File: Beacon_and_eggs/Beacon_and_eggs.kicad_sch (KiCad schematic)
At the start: 41 parts, among them J1 USB_C_Receptacle_USB2.0_16P, Q1 IRLML0030, SW1 Boot, SW2 Reset, U1 SA818V, U2 STM32F411CEUx, U3 ADXL343, U6 MCP1253-33X50I/MS, U7 MCP1253-33X50I/MS, Y1 25MHz 18pF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

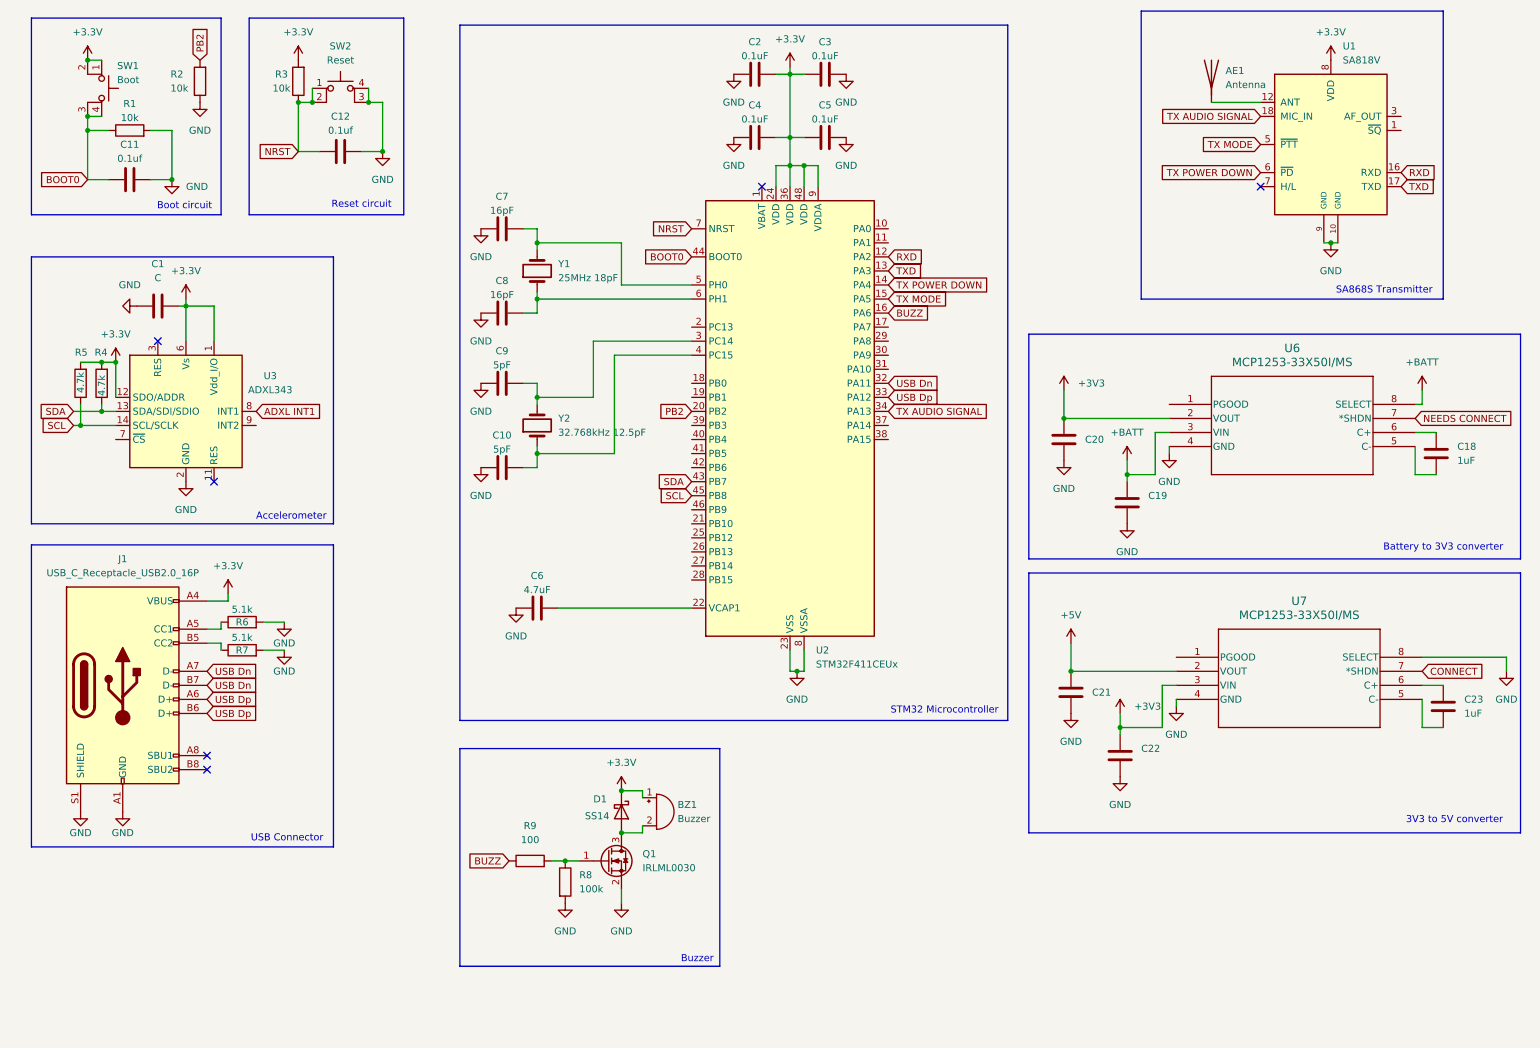
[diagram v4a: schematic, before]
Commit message: relabeled some global tags
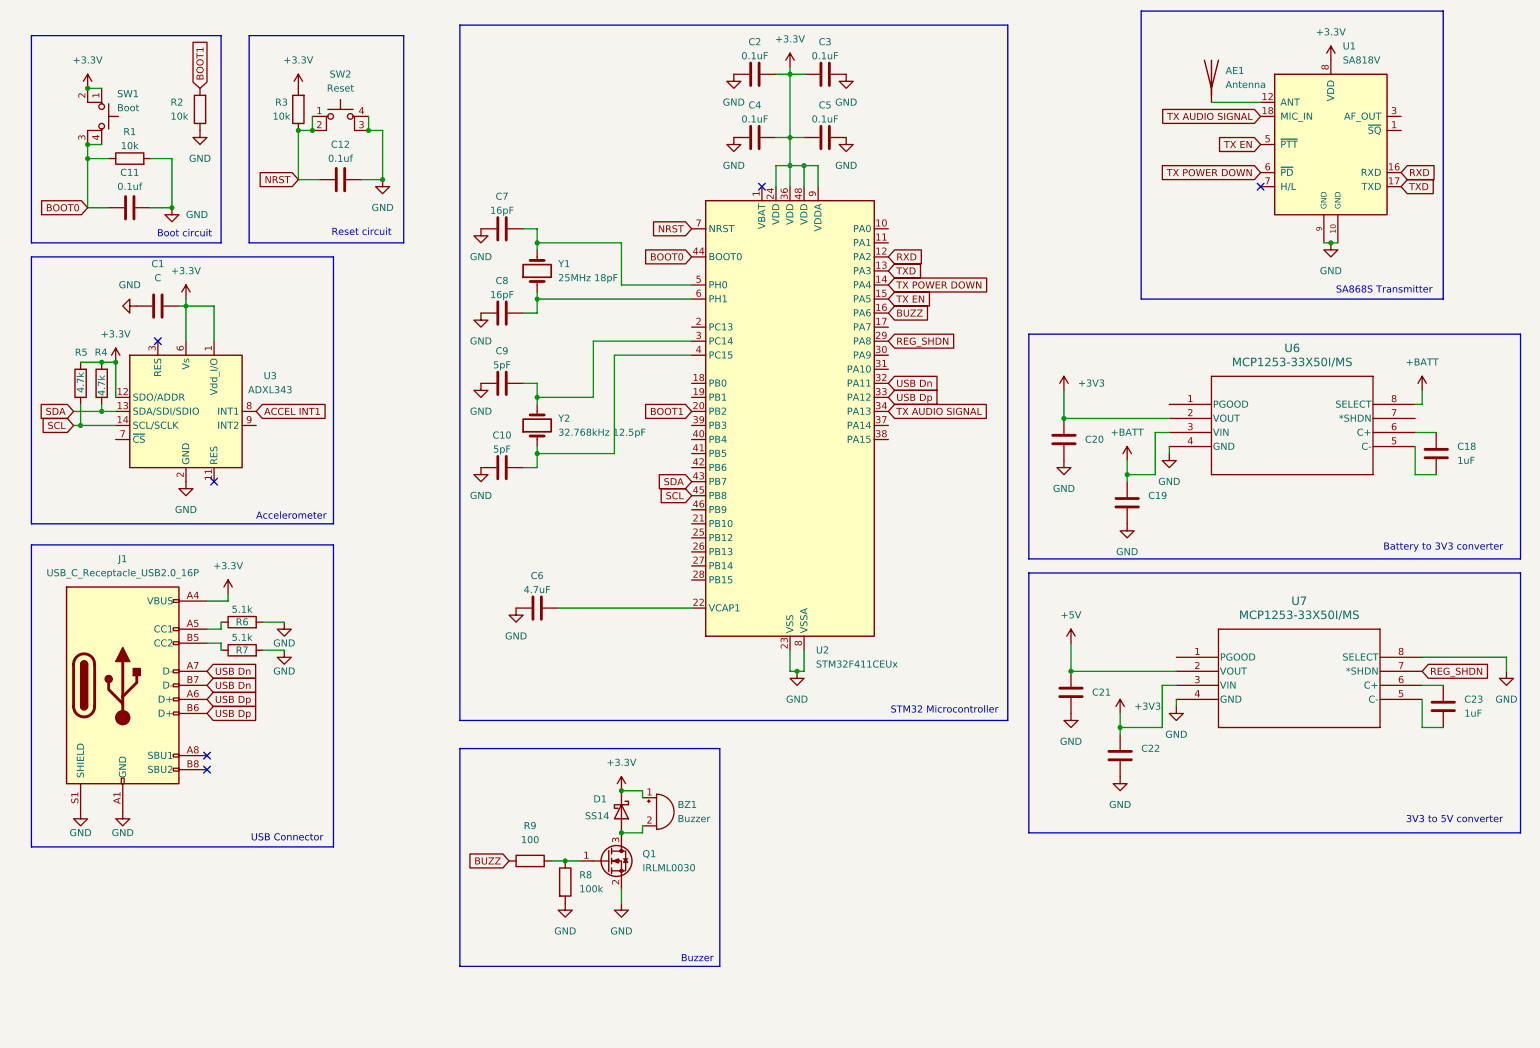
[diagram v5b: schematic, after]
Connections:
- net CONNECT is gone; now on net REG_SHDN: U7.7 (*SHDN)
- net REG_SHDN: now reaches U2.29 (PA8)
- net ADXL INT1 renamed ACCEL INT1
- net NEEDS CONNECT: no longer names the net of U6.7 (*SHDN)
- net PB2 renamed BOOT1
- net TX MODE renamed TX EN
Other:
- moved on the sheet: C11, C12, R1, R2, R3, SW1, SW2

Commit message: Assingned most components(1206 for resistors and Capacitors)
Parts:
- BZ1: footprint (none) -> Buzzer_Beeper:MagneticBuzzer_PUI_SMT-1028-T-2-R
- C1, C10, C11, C12, C2, C3, C4, C5, C6, C7, C8, C9: footprint (none) -> Capacitor_SMD:C_1206_3216Metric
- J1: footprint (none) -> Connector_USB:USB_C_Receptacle_HCTL_HC-TYPE-C-16P-01A
- R1, R2, R3, R4, R5, R6, R7, R8, R9: footprint (none) -> Resistor_SMD:R_1206_3216Metric
- SW1, SW2: footprint (none) -> Button_Switch_SMD:SW_SPST_PTS810
- U6, U7: footprint MSOP8_MC_MCH -> 2025_26-UVR-Beacon:MSOP8_MC_MCH
- renumbered C19 to C13, C18 to C14, C20 to C15, C22 to C16, C23 to C17, C21 to C18
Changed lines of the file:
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@@
 			)
 		)
-		(property "Footprint" ""
+		(property "Footprint" "Capacitor_SMD:C_1206_3216Metric"
 			(at 109.22 119.6848 0)
 			(effects
@@
 			)
 		)
-		(property "Footprint" "MSOP8_MC_MCH"
+		(property "Footprint" "2025_26-UVR-Beacon:MSOP8_MC_MCH"
 			(at 212.598 118.872 0)
 			(effects
@@
 			)
 		)
-		(property "Footprint" ""
+		(property "Footprint" "Resistor_SMD:R_1206_3216Metric"
 			(at 28.448 80.01 90)
 			(effects
@@
 			)
 		)
-		(property "Footprint" ""
+		(property "Footprint" "Connector_USB:USB_C_Receptacle_HCTL_HC-TYPE-C-16P-01A"
 			(at 34.29 134.62 0)
 			(effects
@@
 			)
 		)
-		(property "Footprint" ""
+		(property "Footprint" "Resistor_SMD:R_1206_3216Metric"
 			(at 31.75 41.148 90)
 			(effects
@@
 			)
 		)
-		(property "Footprint" ""
+		(property "Footprint" "Capacitor_SMD:C_1206_3216Metric"
 			(at 148.59 34.5948 0)
 			(effects
@@
 			)
 		)
-		(property "Footprint" ""
+		(property "Footprint" "Resistor_SMD:R_1206_3216Metric"
 			(at 52.07 130.048 90)
 			(effects
@@
 			)
 		)
-		(property "Footprint" ""
+		(property "Footprint" "Capacitor_SMD:C_1206_3216Metric"
 			(at 40.64 65.0748 0)
 			(effects
@@
 		(dnp no)
 		(fields_autoplaced yes)
-		(property "Reference" "C19"
-			(at 215.9 100.3299 0)
+		(property "Reference" "C13"
+			(at 215.9 101.5999 0)
 			(effects
 				(font
@@
 			(project "Beacon_and_eggs"
 				(path "/8792c0a0-2ad2-47f4-a55d-c9a646f00347"
-					(reference "C19")
+					(reference "C13")
 					(unit 1)
 				)
@@
 			)
 		)
-		(property "Footprint" ""
+		(property "Footprint" "Resistor_SMD:R_1206_3216Metric"
 			(at 24.638 80.01 90)
 			(effects
@@
 		(dnp no)
 		(fields_autoplaced yes)
-		(property "Reference" "C20"
+		(property "Reference" "C15"
 			(at 204.47 90.1699 0)
 			(effects
@@
 			(project "Beacon_and_eggs"
 				(path "/8792c0a0-2ad2-47f4-a55d-c9a646f00347"
-					(reference "C20")
+					(reference "C15")
 					(unit 1)
 				)
@@
 			)
 		)
-		(property "Footprint" ""
+		(property "Footprint" "Capacitor_SMD:C_1206_3216Metric"
 			(at 161.29 34.5948 0)
 			(effects
@@
 		(dnp no)
 		(fields_autoplaced yes)
-		(property "Reference" "C22"
-			(at 214.63 146.0499 0)
+		(property "Reference" "C16"
+			(at 214.63 147.3199 0)
 			(effects
 				(font
@@
 			(project "Beacon_and_eggs"
 				(path "/8792c0a0-2ad2-47f4-a55d-c9a646f00347"
-					(reference "C22")
+					(reference "C16")
 					(unit 1)
 				)
@@
 			)
 		)
-		(property "Footprint" ""
+		(property "Footprint" "Capacitor_SMD:C_1206_3216Metric"
 			(at 35.56 47.2948 0)
 			(effects
@@
 		(dnp no)
 		(fields_autoplaced yes)
-		(property "Reference" "C21"
+		(property "Reference" "C18"
 			(at 205.74 135.8899 0)
 			(effects
@@
 			(project "Beacon_and_eggs"
 				(path "/8792c0a0-2ad2-47f4-a55d-c9a646f00347"
-					(reference "C21")
+					(reference "C18")
 					(unit 1)
 				)
@@
 			)
 		)
-		(property "Footprint" ""
+		(property "Footprint" "Resistor_SMD:R_1206_3216Metric"
 			(at 64.008 30.48 90)
 			(effects
@@
 			)
 		)
-		(property "Footprint" ""
+		(property "Footprint" "Capacitor_SMD:C_1206_3216Metric"
 			(at 148.59 23.1648 0)
 			(effects
@@
 			)
 		)
-		(property "Footprint" ""
+		(property "Footprint" "Resistor_SMD:R_1206_3216Metric"
 			(at 108.712 170.18 90)
 			(effects
@@
 		(dnp no)
 		(fields_autoplaced yes)
-		(property "Reference" "C23"
+		(property "Reference" "C17"
 			(at 273.05 137.1599 0)
 			(effects
@@
 			(project "Beacon_and_eggs"
 				(path "/8792c0a0-2ad2-47f4-a55d-c9a646f00347"
-					(reference "C23")
+					(reference "C17")
 					(unit 1)
 				)
@@
 			)
 		)
-		(property "Footprint" ""
+		(property "Footprint" "Resistor_SMD:R_1206_3216Metric"
 			(at 52.07 124.968 90)
 			(effects
@@
 			)
 		)
-		(property "Footprint" ""
+		(property "Footprint" "Capacitor_SMD:C_1206_3216Metric"
 			(at 102.87 79.0448 0)
 			(effects
@@
 			)
 		)
-		(property "Footprint" ""
+		(property "Footprint" "Capacitor_SMD:C_1206_3216Metric"
 			(at 73.66 42.2148 0)
 			(effects
@@
 		(dnp no)
 		(fields_autoplaced yes)
-		(property "Reference" "C18"
+		(property "Reference" "C14"
 			(at 271.78 91.4399 0)
 			(effects
@@
 			(project "Beacon_and_eggs"
 				(path "/8792c0a0-2ad2-47f4-a55d-c9a646f00347"
-					(reference "C18")
+					(reference "C14")
 					(unit 1)
 				)
@@
 			)
 		)
-		(property "Footprint" ""
+		(property "Footprint" "Capacitor_SMD:C_1206_3216Metric"
 			(at 102.87 51.1048 0)
 			(effects
@@
 			)
 		)
-		(property "Footprint" ""
+		(property "Footprint" "Capacitor_SMD:C_1206_3216Metric"
 			(at 161.29 23.1648 0)
 			(effects
@@
 			)
 		)
-		(property "Footprint" ""
+		(property "Footprint" "Resistor_SMD:R_1206_3216Metric"
 			(at 104.14 168.148 90)
 			(effects
@@
 			)
 		)
-		(property "Footprint" ""
+		(property "Footprint" "Button_Switch_SMD:SW_SPST_PTS810"
 			(at 31.75 31.75 0)
 			(effects
@@
 			)
 		)
-		(property "Footprint" ""
+		(property "Footprint" "Button_Switch_SMD:SW_SPST_PTS810"
 			(at 69.85 26.67 0)
 			(effects
@@
 			)
 		)
-		(property "Footprint" ""
+		(property "Footprint" "Capacitor_SMD:C_1206_3216Metric"
 			(at 102.87 66.3448 0)
 			(effects
@@
 			)
 		)
-		(property "Footprint" ""
+		(property "Footprint" "Buzzer_Beeper:MagneticBuzzer_PUI_SMT-1028-T-2-R"
 			(at 126.365 154.94 90)
 			(effects
@@
 			)
 		)
-		(property "Footprint" ""
+		(property "Footprint" "Resistor_SMD:R_1206_3216Metric"
 			(at 46.228 30.48 90)
 			(effects
@@
 			)
 		)
-		(property "Footprint" ""
+		(property "Footprint" "Capacitor_SMD:C_1206_3216Metric"
 			(at 102.87 94.2848 0)
 			(effects
@@
 			)
 		)
-		(property "Footprint" "MSOP8_MC_MCH"
+		(property "Footprint" "2025_26-UVR-Beacon:MSOP8_MC_MCH"
 			(at 211.328 73.152 0)
 			(effects

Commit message: Revert "Assingned most components(1206 for resistors and Capacitors)"
This reverts commit 7557e7a7bd89896b141ef55f24d0591e6209fe46.
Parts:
- BZ1: footprint Buzzer_Beeper:MagneticBuzzer_PUI_SMT-1028-T-2-R -> (none)
- C1, C10, C11, C12, C2, C3, C4, C5, C6, C7, C8, C9: footprint Capacitor_SMD:C_1206_3216Metric -> (none)
- J1: footprint Connector_USB:USB_C_Receptacle_HCTL_HC-TYPE-C-16P-01A -> (none)
- R1, R2, R3, R4, R5, R6, R7, R8, R9: footprint Resistor_SMD:R_1206_3216Metric -> (none)
- SW1, SW2: footprint Button_Switch_SMD:SW_SPST_PTS810 -> (none)
- U6, U7: footprint 2025_26-UVR-Beacon:MSOP8_MC_MCH -> MSOP8_MC_MCH
- renumbered C14 to C18, C13 to C19, C15 to C20, C18 to C21, C16 to C22, C17 to C23
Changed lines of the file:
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@@
 			)
 		)
-		(property "Footprint" "Capacitor_SMD:C_1206_3216Metric"
+		(property "Footprint" ""
 			(at 109.22 119.6848 0)
 			(effects
@@
 			)
 		)
-		(property "Footprint" "2025_26-UVR-Beacon:MSOP8_MC_MCH"
+		(property "Footprint" "MSOP8_MC_MCH"
 			(at 212.598 118.872 0)
 			(effects
@@
 			)
 		)
-		(property "Footprint" "Resistor_SMD:R_1206_3216Metric"
+		(property "Footprint" ""
 			(at 28.448 80.01 90)
 			(effects
@@
 			)
 		)
-		(property "Footprint" "Connector_USB:USB_C_Receptacle_HCTL_HC-TYPE-C-16P-01A"
+		(property "Footprint" ""
 			(at 34.29 134.62 0)
 			(effects
@@
 			)
 		)
-		(property "Footprint" "Resistor_SMD:R_1206_3216Metric"
+		(property "Footprint" ""
 			(at 31.75 41.148 90)
 			(effects
@@
 			)
 		)
-		(property "Footprint" "Capacitor_SMD:C_1206_3216Metric"
+		(property "Footprint" ""
 			(at 148.59 34.5948 0)
 			(effects
@@
 			)
 		)
-		(property "Footprint" "Resistor_SMD:R_1206_3216Metric"
+		(property "Footprint" ""
 			(at 52.07 130.048 90)
 			(effects
@@
 			)
 		)
-		(property "Footprint" "Capacitor_SMD:C_1206_3216Metric"
+		(property "Footprint" ""
 			(at 40.64 65.0748 0)
 			(effects
@@
 		(dnp no)
 		(fields_autoplaced yes)
-		(property "Reference" "C13"
-			(at 215.9 101.5999 0)
+		(property "Reference" "C19"
+			(at 215.9 100.3299 0)
 			(effects
 				(font
@@
 			(project "Beacon_and_eggs"
 				(path "/8792c0a0-2ad2-47f4-a55d-c9a646f00347"
-					(reference "C13")
+					(reference "C19")
 					(unit 1)
 				)
@@
 			)
 		)
-		(property "Footprint" "Resistor_SMD:R_1206_3216Metric"
+		(property "Footprint" ""
 			(at 24.638 80.01 90)
 			(effects
@@
 		(dnp no)
 		(fields_autoplaced yes)
-		(property "Reference" "C15"
+		(property "Reference" "C20"
 			(at 204.47 90.1699 0)
 			(effects
@@
 			(project "Beacon_and_eggs"
 				(path "/8792c0a0-2ad2-47f4-a55d-c9a646f00347"
-					(reference "C15")
+					(reference "C20")
 					(unit 1)
 				)
@@
 			)
 		)
-		(property "Footprint" "Capacitor_SMD:C_1206_3216Metric"
+		(property "Footprint" ""
 			(at 161.29 34.5948 0)
 			(effects
@@
 		(dnp no)
 		(fields_autoplaced yes)
-		(property "Reference" "C16"
-			(at 214.63 147.3199 0)
+		(property "Reference" "C22"
+			(at 214.63 146.0499 0)
 			(effects
 				(font
@@
 			(project "Beacon_and_eggs"
 				(path "/8792c0a0-2ad2-47f4-a55d-c9a646f00347"
-					(reference "C16")
+					(reference "C22")
 					(unit 1)
 				)
@@
 			)
 		)
-		(property "Footprint" "Capacitor_SMD:C_1206_3216Metric"
+		(property "Footprint" ""
 			(at 35.56 47.2948 0)
 			(effects
@@
 		(dnp no)
 		(fields_autoplaced yes)
-		(property "Reference" "C18"
+		(property "Reference" "C21"
 			(at 205.74 135.8899 0)
 			(effects
@@
 			(project "Beacon_and_eggs"
 				(path "/8792c0a0-2ad2-47f4-a55d-c9a646f00347"
-					(reference "C18")
+					(reference "C21")
 					(unit 1)
 				)
@@
 			)
 		)
-		(property "Footprint" "Resistor_SMD:R_1206_3216Metric"
+		(property "Footprint" ""
 			(at 64.008 30.48 90)
 			(effects
@@
 			)
 		)
-		(property "Footprint" "Capacitor_SMD:C_1206_3216Metric"
+		(property "Footprint" ""
 			(at 148.59 23.1648 0)
 			(effects
@@
 			)
 		)
-		(property "Footprint" "Resistor_SMD:R_1206_3216Metric"
+		(property "Footprint" ""
 			(at 108.712 170.18 90)
 			(effects
@@
 		(dnp no)
 		(fields_autoplaced yes)
-		(property "Reference" "C17"
+		(property "Reference" "C23"
 			(at 273.05 137.1599 0)
 			(effects
@@
 			(project "Beacon_and_eggs"
 				(path "/8792c0a0-2ad2-47f4-a55d-c9a646f00347"
-					(reference "C17")
+					(reference "C23")
 					(unit 1)
 				)
@@
 			)
 		)
-		(property "Footprint" "Resistor_SMD:R_1206_3216Metric"
+		(property "Footprint" ""
 			(at 52.07 124.968 90)
 			(effects
@@
 			)
 		)
-		(property "Footprint" "Capacitor_SMD:C_1206_3216Metric"
+		(property "Footprint" ""
 			(at 102.87 79.0448 0)
 			(effects
@@
 			)
 		)
-		(property "Footprint" "Capacitor_SMD:C_1206_3216Metric"
+		(property "Footprint" ""
 			(at 73.66 42.2148 0)
 			(effects
@@
 		(dnp no)
 		(fields_autoplaced yes)
-		(property "Reference" "C14"
+		(property "Reference" "C18"
 			(at 271.78 91.4399 0)
 			(effects
@@
 			(project "Beacon_and_eggs"
 				(path "/8792c0a0-2ad2-47f4-a55d-c9a646f00347"
-					(reference "C14")
+					(reference "C18")
 					(unit 1)
 				)
@@
 			)
 		)
-		(property "Footprint" "Capacitor_SMD:C_1206_3216Metric"
+		(property "Footprint" ""
 			(at 102.87 51.1048 0)
 			(effects
@@
 			)
 		)
-		(property "Footprint" "Capacitor_SMD:C_1206_3216Metric"
+		(property "Footprint" ""
 			(at 161.29 23.1648 0)
 			(effects
@@
 			)
 		)
-		(property "Footprint" "Resistor_SMD:R_1206_3216Metric"
+		(property "Footprint" ""
 			(at 104.14 168.148 90)
 			(effects
@@
 			)
 		)
-		(property "Footprint" "Button_Switch_SMD:SW_SPST_PTS810"
+		(property "Footprint" ""
 			(at 31.75 31.75 0)
 			(effects
@@
 			)
 		)
-		(property "Footprint" "Button_Switch_SMD:SW_SPST_PTS810"
+		(property "Footprint" ""
 			(at 69.85 26.67 0)
 			(effects
@@
 			)
 		)
-		(property "Footprint" "Capacitor_SMD:C_1206_3216Metric"
+		(property "Footprint" ""
 			(at 102.87 66.3448 0)
 			(effects
@@
 			)
 		)
-		(property "Footprint" "Buzzer_Beeper:MagneticBuzzer_PUI_SMT-1028-T-2-R"
+		(property "Footprint" ""
 			(at 126.365 154.94 90)
 			(effects
@@
 			)
 		)
-		(property "Footprint" "Resistor_SMD:R_1206_3216Metric"
+		(property "Footprint" ""
 			(at 46.228 30.48 90)
 			(effects
@@
 			)
 		)
-		(property "Footprint" "Capacitor_SMD:C_1206_3216Metric"
+		(property "Footprint" ""
 			(at 102.87 94.2848 0)
 			(effects
@@
 			)
 		)
-		(property "Footprint" "2025_26-UVR-Beacon:MSOP8_MC_MCH"
+		(property "Footprint" "MSOP8_MC_MCH"
 			(at 211.328 73.152 0)
 			(effects
